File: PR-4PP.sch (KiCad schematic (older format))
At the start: 28 parts, among them J1 USB_C_Receptacle_USB2.0, SW1 SW_Push, U1 ATmega32U4-AU, U3 SRV05-4, Y1 16mHz

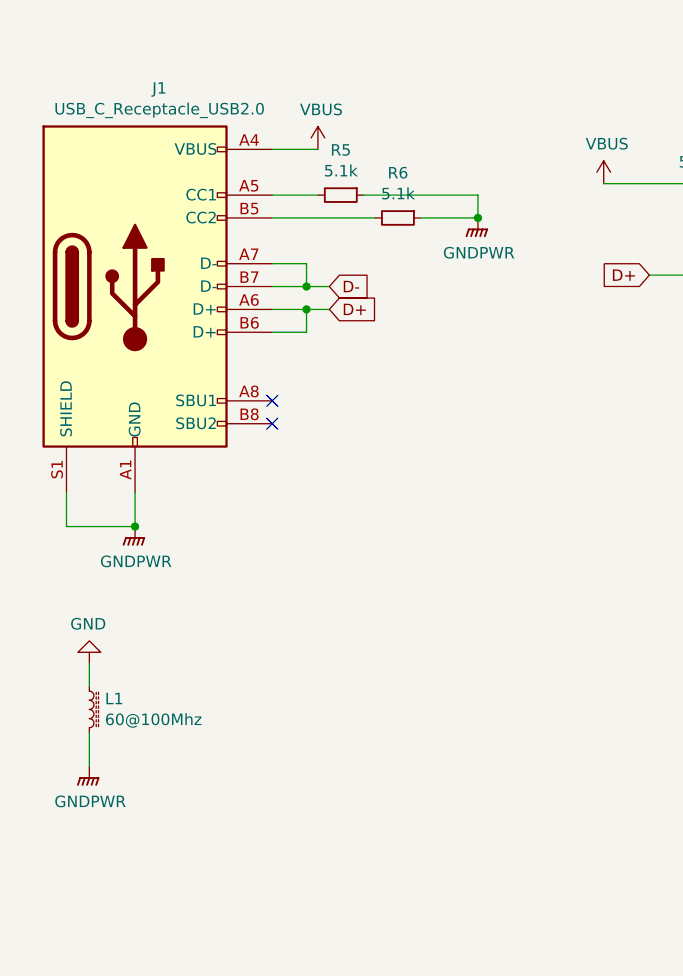
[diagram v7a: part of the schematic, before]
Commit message: add submodule & implement new footprint
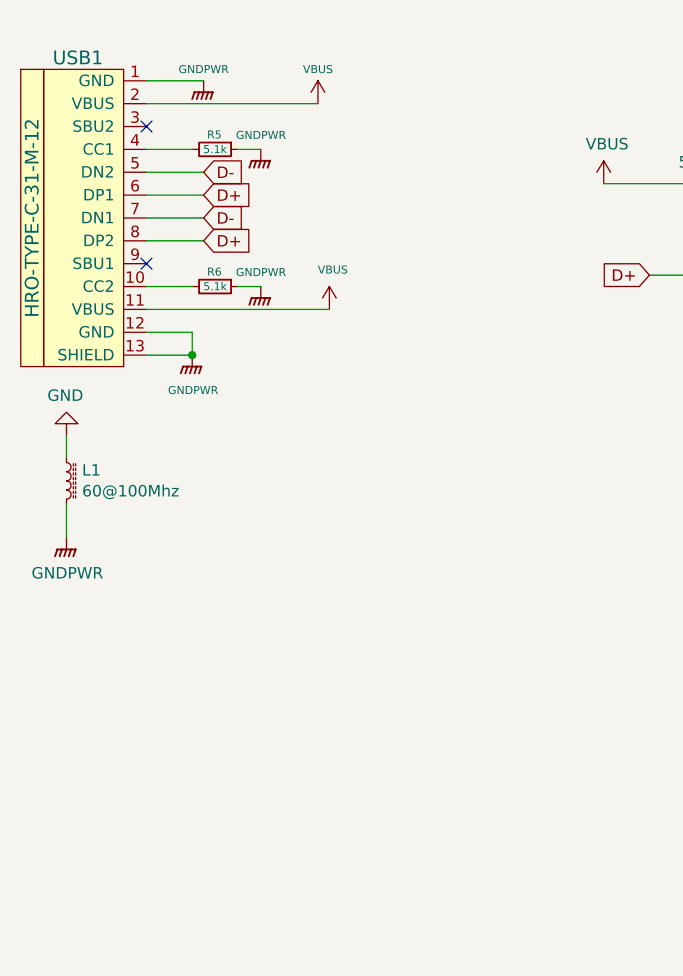
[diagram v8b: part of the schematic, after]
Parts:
- removed J1: USB_C_Receptacle_USB2.0, symbol Connector:USB_C_Receptacle_USB2.0
- added USB1: HRO-TYPE-C-31-M-12, symbol Type-C:HRO-TYPE-C-31-M-12
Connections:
- net D+: now also USB1.6 (DP1), USB1.8 (DP2)
- net D-: now also USB1.5 (DN2), USB1.7 (DN1)
- net GNDPWR: now also USB1.1 (GND), USB1.12 (GND), USB1.13 (SHIELD)
- net VBUS: now also USB1.11 (VBUS), USB1.2 (VBUS)
- net at R5.2: now also USB1.4 (CC1)
- net at R6.2: now also USB1.10 (CC2)
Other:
- moved on the sheet: L1, R6
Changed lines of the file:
@@
 L power:VBUS #PWR0111
 U 1 1 6170BDF8
-P 2250 1400
-F 0 "#PWR0111" H 2250 1250 50  0001 C CNN
-F 1 "VBUS" H 2265 1573 50  0000 C CNN
-F 2 "" H 2250 1400 50  0001 C CNN
-F 3 "" H 2250 1400 50  0001 C CNN
-	1    2250 1400
-	1    0    0    -1
-$EndComp
-$Comp
-L Device:R_Small R5
-U 1 1 6171101F
-P 2350 1600
-F 0 "R5" V 2154 1600 50  0000 C CNN
-F 1 "5.1k" V 2245 1600 50  0000 C CNN
-F 2 "Capacitor_SMD:C_0805_2012Metric_Pad1.15x1.40mm_HandSolder" H 2350 1600 50  0001 C CNN
-F 3 "~" H 2350 1600 50  0001 C CNN
-	1    2350 1600
-	0    1    1    0
-$EndComp
-Wire Wire Line
-	2050 1600 2250 1600
-$Comp
-L Device:R_Small R6
-U 1 1 61713A4B
-P 2600 1700
-F 0 "R6" V 2404 1700 50  0000 C CNN
-F 1 "5.1k" V 2495 1700 50  0000 C CNN
-F 2 "Capacitor_SMD:C_0805_2012Metric_Pad1.15x1.40mm_HandSolder" H 2600 1700 50  0001 C CNN
-F 3 "~" H 2600 1700 50  0001 C CNN
-	1    2600 1700
-	0    1    1    0
-$EndComp
-Wire Wire Line
-	2050 1700 2500 1700
+P 2250 1200
+F 0 "#PWR0111" H 2250 1050 50  0001 C CNN
+F 1 "VBUS" H 2250 1350 35  0000 C CNN
+F 2 "" H 2250 1200 50  0001 C CNN
+F 3 "" H 2250 1200 50  0001 C CNN
+	1    2250 1200
+	1    0    0    -1
+$EndComp
+Wire Wire Line
+	1500 2000 1700 2000
 $Comp
 L power:GNDPWR #PWR0112
 U 1 1 61717B5D
-P 2950 1700
-F 0 "#PWR0112" H 2950 1500 50  0001 C CNN
-F 1 "GNDPWR" H 2954 1546 50  0000 C CNN
-F 2 "" H 2950 1650 50  0001 C CNN
-F 3 "" H 2950 1650 50  0001 C CNN
-	1    2950 1700
-	1    0    0    -1
-$EndComp
-Wire Wire Line
-	2700 1700 2950 1700
-Wire Wire Line
-	2450 1600 2950 1600
-Wire Wire Line
-	2950 1600 2950 1700
-Connection ~ 2950 1700
-NoConn ~ 2050 2500
-NoConn ~ 2050 2600
-$Comp
-L power:GNDPWR #PWR0113
-U 1 1 6171D868
-P 1450 3050
-F 0 "#PWR0113" H 1450 2850 50  0001 C CNN
-F 1 "GNDPWR" H 1454 2896 50  0000 C CNN
-F 2 "" H 1450 3000 50  0001 C CNN
-F 3 "" H 1450 3000 50  0001 C CNN
-	1    1450 3050
-	1    0    0    -1
-$EndComp
-Wire Wire Line
-	1450 2900 1450 3050
-Wire Wire Line
-	1450 3050 1150 3050
-Wire Wire Line
-	1150 3050 1150 2900
-Connection ~ 1450 3050
+P 1700 2300
+F 0 "#PWR0112" H 1700 2100 50  0001 C CNN
+F 1 "GNDPWR" H 1704 2146 35  0000 C CNN
+F 2 "" H 1700 2250 50  0001 C CNN
+F 3 "" H 1700 2250 50  0001 C CNN
+	1    1700 2300
+	1    0    0    -1
+$EndComp
+Wire Wire Line
+	1500 2300 1700 2300
+Wire Wire Line
+	1500 2200 1700 2200
+Wire Wire Line
+	1700 2200 1700 2300
+Connection ~ 1700 2300
 $Comp
 L Device:L_Core_Ferrite_Small L1
 U 1 1 6172C389
-P 1250 3850
-F 0 "L1" H 1318 3896 50  0000 L CNN
-F 1 "60@100Mhz" H 1318 3805 50  0000 L CNN
-F 2 "Inductor_SMD:L_1206_3216Metric_Pad1.42x1.75mm_HandSolder" H 1250 3850 50  0001 C CNN
-F 3 "~" H 1250 3850 50  0001 C CNN
-	1    1250 3850
+P 1150 2850
+F 0 "L1" H 1218 2896 50  0000 L CNN
+F 1 "60@100Mhz" H 1218 2805 50  0000 L CNN
+F 2 "Inductor_SMD:L_1206_3216Metric_Pad1.42x1.75mm_HandSolder" H 1150 2850 50  0001 C CNN
+F 3 "~" H 1150 2850 50  0001 C CNN
+	1    1150 2850
 	1    0    0    -1
 $EndComp
@@
 L power:GND #PWR0114
 U 1 1 6172D0C5
-P 1250 3650
-F 0 "#PWR0114" H 1250 3400 50  0001 C CNN
-F 1 "GND" H 1255 3477 50  0000 C CNN
-F 2 "" H 1250 3650 50  0001 C CNN
-F 3 "" H 1250 3650 50  0001 C CNN
-	1    1250 3650
+P 1150 2650
+F 0 "#PWR0114" H 1150 2400 50  0001 C CNN
+F 1 "GND" H 1155 2477 50  0000 C CNN
+F 2 "" H 1150 2650 50  0001 C CNN
+F 3 "" H 1150 2650 50  0001 C CNN
+	1    1150 2650
 	-1   0    0    1
 $EndComp
 Wire Wire Line
-	1250 3650 1250 3750
+	1150 2650 1150 2750
 $Comp
 L power:GNDPWR #PWR0115
 U 1 1 6172F9F8
-P 1250 4100
-F 0 "#PWR0115" H 1250 3900 50  0001 C CNN
-F 1 "GNDPWR" H 1254 3946 50  0000 C CNN
-F 2 "" H 1250 4050 50  0001 C CNN
-F 3 "" H 1250 4050 50  0001 C CNN
-	1    1250 4100
-	1    0    0    -1
-$EndComp
-Wire Wire Line
-	1250 4100 1250 3950
+P 1150 3100
+F 0 "#PWR0115" H 1150 2900 50  0001 C CNN
+F 1 "GNDPWR" H 1154 2946 50  0000 C CNN
+F 2 "" H 1150 3050 50  0001 C CNN
+F 3 "" H 1150 3050 50  0001 C CNN
+	1    1150 3100
+	1    0    0    -1
+$EndComp
+Wire Wire Line
+	1150 3100 1150 2950
 Text Notes 7350 7500 0    50   ~ 0
 PR-4PP (ai03 guide w/ usb c)
@@
 Wire Wire Line
 	3500 1550 3850 1550
-Text GLabel 2300 2000 2    50   Input ~ 0
+Text GLabel 1750 1700 2    50   Input ~ 0
 D-
-Wire Wire Line
-	2050 2000 2200 2000
-Wire Wire Line
-	2050 1900 2200 1900
-Wire Wire Line
-	2200 1900 2200 2000
-Connection ~ 2200 2000
-Wire Wire Line
-	2200 2000 2300 2000
-Text GLabel 2300 2100 2    50   Input ~ 0
+Text GLabel 1750 1800 2    50   Input ~ 0
 D+
-Wire Wire Line
-	2050 2100 2200 2100
-Wire Wire Line
-	2050 2200 2200 2200
-Wire Wire Line
-	2200 2200 2200 2100
-Connection ~ 2200 2100
-Wire Wire Line
-	2200 2100 2300 2100
 Text GLabel 3700 1950 0    50   Input ~ 0
 D+
@@
 Wire Wire Line
 	10600 1250 10600 1050
-$Comp
-L Connector:USB_C_Receptacle_USB2.0 J1
-U 1 1 61707A88
-P 1450 2000
-F 0 "J1" H 1557 2867 50  0000 C CNN
-F 1 "USB_C_Receptacle_USB2.0" H 1557 2776 50  0000 C CNN
-F 2 "" H 1600 2000 50  0001 C CNN
-F 3 "https://www.usb.org/sites/default/files/documents/usb_type-c.zip" H 1600 2000 50  0001 C CNN
-	1    1450 2000
-	1    0    0    -1
-$EndComp
-Wire Wire Line
-	2050 1400 2250 1400
+Wire Wire Line
+	1500 1200 2250 1200
 Wire Wire Line
 	7550 2300 7550 2450
+$Comp
+L Type-C:HRO-TYPE-C-31-M-12 USB1
+U 1 1 6194D03A
+P 1400 1650
+F 0 "USB1" H 1200 2300 60  0000 C CNN
+F 1 "HRO-TYPE-C-31-M-12" V 1000 1600 60  0000 C CNN
+F 2 "" H 1400 1650 60  0001 C CNN
+F 3 "" H 1400 1650 60  0001 C CNN
+	1    1400 1650
+	1    0    0    -1
+$EndComp
+$Comp
+L power:VBUS #PWR0113
+U 1 1 61970D59
+P 2300 2100
+F 0 "#PWR0113" H 2300 1950 50  0001 C CNN
+F 1 "VBUS" H 2315 2273 35  0000 C CNN
+F 2 "" H 2300 2100 50  0001 C CNN
+F 3 "" H 2300 2100 50  0001 C CNN
+	1    2300 2100
+	1    0    0    -1
+$EndComp
+Wire Wire Line
+	1500 2100 2300 2100
+$Comp
+L Device:R_Small R6
+U 1 1 61713A4B
+P 1800 2000
+F 0 "R6" V 1736 1997 35  0000 C CNN
+F 1 "5.1k" V 1800 2000 35  0000 C CNN
+F 2 "Capacitor_SMD:C_0805_2012Metric_Pad1.15x1.40mm_HandSolder" H 1800 2000 50  0001 C CNN
+F 3 "~" H 1800 2000 50  0001 C CNN
+	1    1800 2000
+	0    1    1    0
+$EndComp
+Wire Wire Line
+	1500 1400 1700 1400
+Wire Wire Line
+	1500 1800 1750 1800
+Wire Wire Line
+	1500 1700 1750 1700
+Text GLabel 1750 1500 2    50   Input ~ 0
+D-
+Text GLabel 1750 1600 2    50   Input ~ 0
+D+
+Wire Wire Line
+	1500 1600 1750 1600
+Wire Wire Line
+	1500 1500 1750 1500
+NoConn ~ 1500 1300
+$Comp
+L power:GNDPWR #PWR0123
+U 1 1 619953F6
+P 1750 1100
+F 0 "#PWR0123" H 1750 900 50  0001 C CNN
+F 1 "GNDPWR" H 1750 1150 35  0000 C CNN
+F 2 "" H 1750 1050 50  0001 C CNN
+F 3 "" H 1750 1050 50  0001 C CNN
+	1    1750 1100
+	1    0    0    -1
+$EndComp
+Wire Wire Line
+	1500 1100 1750 1100
+NoConn ~ 1500 1900
+$Comp
+L power:GNDPWR #PWR0124
+U 1 1 619AEDC1
+P 2000 2000
+F 0 "#PWR0124" H 2000 1800 50  0001 C CNN
+F 1 "GNDPWR" H 2001 2062 35  0000 C CNN
+F 2 "" H 2000 1950 50  0001 C CNN
+F 3 "" H 2000 1950 50  0001 C CNN
+	1    2000 2000
+	1    0    0    -1
+$EndComp
+Wire Wire Line
+	2000 2000 1900 2000
+$Comp
+L power:GNDPWR #PWR0125
+U 1 1 619CA276
+P 2000 1400
+F 0 "#PWR0125" H 2000 1200 50  0001 C CNN
+F 1 "GNDPWR" H 2001 1462 35  0000 C CNN
+F 2 "" H 2000 1350 50  0001 C CNN
+F 3 "" H 2000 1350 50  0001 C CNN
+	1    2000 1400
+	1    0    0    -1
+$EndComp
+Wire Wire Line
+	2000 1400 1900 1400
+$Comp
+L Device:R_Small R5
+U 1 1 619CEFB2
+P 1800 1400
+F 0 "R5" V 1736 1397 35  0000 C CNN
+F 1 "5.1k" V 1800 1400 35  0000 C CNN
+F 2 "Capacitor_SMD:C_0805_2012Metric_Pad1.15x1.40mm_HandSolder" H 1800 1400 50  0001 C CNN
+F 3 "~" H 1800 1400 50  0001 C CNN
+	1    1800 1400
+	0    1    1    0
+$EndComp
 $EndSCHEMATC
